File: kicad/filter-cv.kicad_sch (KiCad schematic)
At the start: 21 parts, among them Q11 2N3906, Q12 2N3904, Q13 2N3906, U18 TL074

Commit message: component positioning mostly done
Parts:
- C55, C56: footprint rumblesan-standard-parts:C_Rect_L7.0mm_W3.5mm_P5.00mm -> rumblesan-standard-parts:C_Rect_L7.0mm_W2.5mm_P5.00mm
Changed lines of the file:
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@@
       (effects (font (size 1.27 1.27)) (justify left))
     )
-    (property "Footprint" "rumblesan-standard-parts:C_Rect_L7.0mm_W3.5mm_P5.00mm" (id 2) (at 197.485 63.5 90)
+    (property "Footprint" "rumblesan-standard-parts:C_Rect_L7.0mm_W2.5mm_P5.00mm" (id 2) (at 197.485 63.5 90)
       (effects (font (size 1.27 1.27)) hide)
     )
@@
       (effects (font (size 1.27 1.27)) (justify left))
     )
-    (property "Footprint" "rumblesan-standard-parts:C_Rect_L7.0mm_W3.5mm_P5.00mm" (id 2) (at 197.485 76.2 90)
-      (effects (font (size 1.27 1.27)) hide)
-    )
+    (property "Footprint" "rumblesan-standard-parts:C_Rect_L7.0mm_W2.5mm_P5.00mm" (id 2) (at 197.485 76.2 90)
+      (effects (font (size 1.27 1.27)) hide)
+    )

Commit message: initial layout done
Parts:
- C53, C54: footprint rumblesan-standard-parts:C_Rect_L7.0mm_W3.5mm_P5.00mm -> rumblesan-standard-parts:C_Rect_L7.0mm_W2.5mm_P5.00mm
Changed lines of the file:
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@@
     (property "Reference" "C54" (id 0) (at 95.25 56.3712 90))
     (property "Value" "220pF" (id 1) (at 95.25 58.9081 90))
-    (property "Footprint" "rumblesan-standard-parts:C_Rect_L7.0mm_W3.5mm_P5.00mm" (id 2) (at 93.98 56.515 0)
+    (property "Footprint" "rumblesan-standard-parts:C_Rect_L7.0mm_W2.5mm_P5.00mm" (id 2) (at 93.98 56.515 0)
       (effects (font (size 1.27 1.27)) hide)
     )
@@
     (property "Reference" "C53" (id 0) (at 90.17 116.0612 90))
     (property "Value" "10nF" (id 1) (at 90.17 118.5981 90))
-    (property "Footprint" "rumblesan-standard-parts:C_Rect_L7.0mm_W3.5mm_P5.00mm" (id 2) (at 88.9 116.205 0)
-      (effects (font (size 1.27 1.27)) hide)
-    )
+    (property "Footprint" "rumblesan-standard-parts:C_Rect_L7.0mm_W2.5mm_P5.00mm" (id 2) (at 88.9 116.205 0)
+      (effects (font (size 1.27 1.27)) hide)
+    )

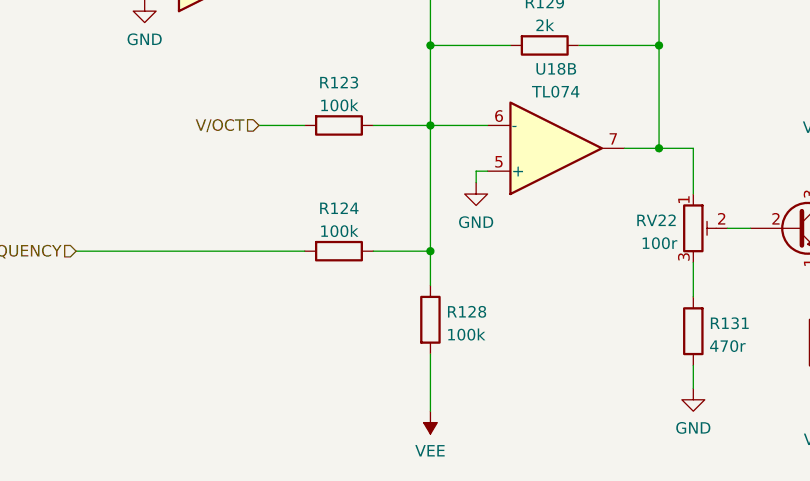
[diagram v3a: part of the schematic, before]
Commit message: Full rejig to use attiny for divider
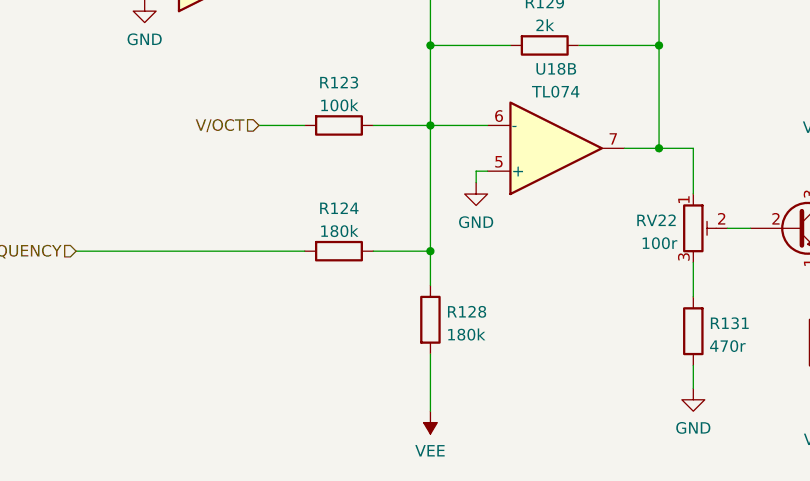
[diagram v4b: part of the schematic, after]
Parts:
- C55, C56: Spec ceramic C0G -> ceramic X7R
- R124, R128: value 100k -> 180k
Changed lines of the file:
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@@
       (effects (font (size 1.27 1.27)) hide)
     )
-    (property "Spec" "ceramic C0G" (id 4) (at 195.58 64.77 90)
+    (property "Spec" "ceramic X7R" (id 4) (at 195.58 64.77 90)
       (effects (font (size 1.27 1.27)) hide)
     )
@@
     (in_bom yes) (on_board yes) (fields_autoplaced)
     (property "Reference" "R124" (id 0) (at 67.31 148.9542 90))
-    (property "Value" "100k" (id 1) (at 67.31 151.4911 90))
+    (property "Value" "180k" (id 1) (at 67.31 151.4911 90))
     (property "Footprint" "rumblesan-standard-parts:R_Axial_DIN0207_L6.3mm_D2.5mm_P10.16mm_Horizontal" (id 2) (at 69.85 151.13 90)
       (effects (font (size 1.27 1.27)) hide)
@@
       (effects (font (size 1.27 1.27)) (justify right))
     )
-    (property "Value" "100k" (id 1) (at 79.248 162.9922 0)
+    (property "Value" "180k" (id 1) (at 79.248 162.9922 0)
       (effects (font (size 1.27 1.27)) (justify right))
     )
@@
       (effects (font (size 1.27 1.27)) hide)
     )
-    (property "Spec" "ceramic C0G" (id 4) (at 195.58 77.47 90)
-      (effects (font (size 1.27 1.27)) hide)
-    )
+    (property "Spec" "ceramic X7R" (id 4) (at 195.58 77.47 90)
+      (effects (font (size 1.27 1.27)) hide)
+    )

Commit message: Changing name to the mercurial machine
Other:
- title: (none) -> The Mercurial Machine
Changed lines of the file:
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@@
   (paper "A4")
   (title_block
+    (title "The Mercurial Machine")
+    (date "2023-05-13")
+    (rev "r02")
     (comment 2 "creativecommons.org/licenses/by/4.0/")
     (comment 3 "License: CC BY 4.0")

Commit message: geographically reannotate parts
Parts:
- renumbered C54 to C58, C55 to C59, C53 to C60, C56 to C65, Q12 to Q10, Q13 to Q9, R130 to R114, R131 to R115, R129 to R116, R123 to R119, R132 to R120, R127 to R122, R124 to R123, R121 to R126, R128 to R127, R122 to R128, R126 to R129, U18 to U16
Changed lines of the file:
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@@
   (symbol (lib_id "rumblesan-standard-parts:R") (at 106.68 162.56 0) (unit 1)
     (in_bom yes) (on_board yes) (fields_autoplaced)
-    (property "Reference" "R131" (id 0) (at 108.458 161.7253 0)
+    (property "Reference" "R115" (id 0) (at 108.458 161.7253 0)
       (effects (font (size 1.27 1.27)) (justify left))
     )
@@
   (symbol (lib_id "rumblesan-standard-parts:C") (at 191.77 64.77 0) (unit 1)
     (in_bom yes) (on_board yes) (fields_autoplaced)
-    (property "Reference" "C55" (id 0) (at 194.691 63.9353 0)
+    (property "Reference" "C59" (id 0) (at 194.691 63.9353 0)
       (effects (font (size 1.27 1.27)) (justify left))
     )
@@
   (symbol (lib_id "rumblesan-standard-parts:R") (at 120.65 163.83 0) (unit 1)
     (in_bom yes) (on_board yes) (fields_autoplaced)
-    (property "Reference" "R132" (id 0) (at 122.428 162.9953 0)
+    (property "Reference" "R120" (id 0) (at 122.428 162.9953 0)
       (effects (font (size 1.27 1.27)) (justify left))
     )
@@
   (symbol (lib_id "Amplifier_Operational:TL074") (at 185.42 71.12 0) (unit 5)
     (in_bom yes) (on_board yes) (fields_autoplaced)
-    (property "Reference" "U18" (id 0) (at 183.515 70.2853 0)
+    (property "Reference" "U16" (id 0) (at 183.515 70.2853 0)
       (effects (font (size 1.27 1.27)) (justify left))
     )
@@
   (symbol (lib_id "rumblesan-standard-parts:R") (at 90.17 130.81 90) (unit 1)
     (in_bom yes) (on_board yes) (fields_autoplaced)
-    (property "Reference" "R129" (id 0) (at 90.17 126.0942 90))
+    (property "Reference" "R116" (id 0) (at 90.17 126.0942 90))
     (property "Value" "2k" (id 1) (at 90.17 128.6311 90))
     (property "Footprint" "rumblesan-standard-parts:R_Axial_DIN0207_L6.3mm_D2.5mm_P10.16mm_Horizontal" (id 2) (at 92.71 128.27 90)
@@
   (symbol (lib_id "rumblesan-standard-parts:R") (at 67.31 153.67 90) (unit 1)
     (in_bom yes) (on_board yes) (fields_autoplaced)
-    (property "Reference" "R124" (id 0) (at 67.31 148.9542 90))
+    (property "Reference" "R123" (id 0) (at 67.31 148.9542 90))
     (property "Value" "180k" (id 1) (at 67.31 151.4911 90))
     (property "Footprint" "rumblesan-standard-parts:R_Axial_DIN0207_L6.3mm_D2.5mm_P10.16mm_Horizontal" (id 2) (at 69.85 151.13 90)
@@
   (symbol (lib_id "Amplifier_Operational:TL074") (at 54.61 121.92 0) (mirror x) (unit 3)
     (in_bom yes) (on_board yes) (fields_autoplaced)
-    (property "Reference" "U18" (id 0) (at 54.61 113.1402 0))
+    (property "Reference" "U16" (id 0) (at 54.61 113.1402 0))
     (property "Value" "TL074" (id 1) (at 54.61 115.6771 0))
     (property "Footprint" "rumblesan-standard-parts:DIP-14_W7.62mm_Socket" (id 2) (at 53.34 124.46 0)
@@
   (symbol (lib_id "rumblesan-standard-parts:R") (at 77.47 161.29 180) (unit 1)
     (in_bom yes) (on_board yes) (fields_autoplaced)
-    (property "Reference" "R128" (id 0) (at 79.248 160.4553 0)
+    (property "Reference" "R127" (id 0) (at 79.248 160.4553 0)
       (effects (font (size 1.27 1.27)) (justify right))
     )
@@
   (symbol (lib_id "Amplifier_Operational:TL074") (at 91.44 142.24 0) (mirror x) (unit 2)
     (in_bom yes) (on_board yes) (fields_autoplaced)
-    (property "Reference" "U18" (id 0) (at 91.44 133.4602 0))
+    (property "Reference" "U16" (id 0) (at 91.44 133.4602 0))
     (property "Value" "TL074" (id 1) (at 91.44 135.9971 0))
     (property "Footprint" "rumblesan-standard-parts:DIP-14_W7.62mm_Socket" (id 2) (at 90.17 144.78 0)
@@
   (symbol (lib_id "rumblesan-standard-parts:R") (at 54.61 38.1 90) (unit 1)
     (in_bom yes) (on_board yes) (fields_autoplaced)
-    (property "Reference" "R121" (id 0) (at 54.61 33.3842 90))
+    (property "Reference" "R126" (id 0) (at 54.61 33.3842 90))
     (property "Value" "20k" (id 1) (at 54.61 35.9211 90))
     (property "Footprint" "rumblesan-standard-parts:R_Axial_DIN0207_L6.3mm_D2.5mm_P10.16mm_Horizontal" (id 2) (at 57.15 35.56 90)
@@
   (symbol (lib_id "Transistor_BJT:2N3904") (at 118.11 151.13 0) (unit 1)
     (in_bom yes) (on_board yes) (fields_autoplaced)
-    (property "Reference" "Q12" (id 0) (at 122.9614 150.2953 0)
+    (property "Reference" "Q10" (id 0) (at 122.9614 150.2953 0)
       (effects (font (size 1.27 1.27)) (justify left))
     )
@@
   (symbol (lib_id "rumblesan-standard-parts:R") (at 100.33 52.07 90) (unit 1)
     (in_bom yes) (on_board yes) (fields_autoplaced)
-    (property "Reference" "R130" (id 0) (at 100.33 47.3542 90))
+    (property "Reference" "R114" (id 0) (at 100.33 47.3542 90))
     (property "Value" "20k" (id 1) (at 100.33 49.8911 90))
     (property "Footprint" "rumblesan-standard-parts:R_Axial_DIN0207_L6.3mm_D2.5mm_P10.16mm_Horizontal" (id 2) (at 102.87 49.53 90)
@@
   (symbol (lib_id "rumblesan-standard-parts:C") (at 95.25 62.23 90) (unit 1)
     (in_bom yes) (on_board yes) (fields_autoplaced)
-    (property "Reference" "C54" (id 0) (at 95.25 56.3712 90))
+    (property "Reference" "C58" (id 0) (at 95.25 56.3712 90))
     (property "Value" "220pF" (id 1) (at 95.25 58.9081 90))
     (property "Footprint" "rumblesan-standard-parts:C_Rect_L7.0mm_W2.5mm_P5.00mm" (id 2) (at 93.98 56.515 0)
@@
   (symbol (lib_id "rumblesan-standard-parts:C") (at 191.77 77.47 0) (unit 1)
     (in_bom yes) (on_board yes) (fields_autoplaced)
-    (property "Reference" "C56" (id 0) (at 194.691 76.6353 0)
+    (property "Reference" "C65" (id 0) (at 194.691 76.6353 0)
       (effects (font (size 1.27 1.27)) (justify left))
     )
@@
   (symbol (lib_id "Transistor_BJT:2N3906") (at 133.35 158.75 0) (unit 1)
     (in_bom yes) (on_board yes) (fields_autoplaced)
-    (property "Reference" "Q13" (id 0) (at 138.2014 157.9153 0)
+    (property "Reference" "Q9" (id 0) (at 138.2014 157.9153 0)
       (effects (font (size 1.27 1.27)) (justify left))
     )
@@
   (symbol (lib_id "Amplifier_Operational:TL074") (at 95.25 76.2 0) (mirror x) (unit 1)
     (in_bom yes) (on_board yes) (fields_autoplaced)
-    (property "Reference" "U18" (id 0) (at 95.25 67.4202 0))
+    (property "Reference" "U16" (id 0) (at 95.25 67.4202 0))
     (property "Value" "TL074" (id 1) (at 95.25 69.9571 0))
     (property "Footprint" "rumblesan-standard-parts:DIP-14_W7.62mm_Socket" (id 2) (at 93.98 78.74 0)
@@
   (symbol (lib_id "rumblesan-standard-parts:C") (at 90.17 121.92 90) (unit 1)
     (in_bom yes) (on_board yes) (fields_autoplaced)
-    (property "Reference" "C53" (id 0) (at 90.17 116.0612 90))
+    (property "Reference" "C60" (id 0) (at 90.17 116.0612 90))
     (property "Value" "10nF" (id 1) (at 90.17 118.5981 90))
     (property "Footprint" "rumblesan-standard-parts:C_Rect_L7.0mm_W2.5mm_P5.00mm" (id 2) (at 88.9 116.205 0)
@@
   (symbol (lib_id "Amplifier_Operational:TL074") (at 54.61 53.34 0) (mirror x) (unit 4)
     (in_bom yes) (on_board yes) (fields_autoplaced)
-    (property "Reference" "U18" (id 0) (at 54.61 44.5602 0))
+    (property "Reference" "U16" (id 0) (at 54.61 44.5602 0))
     (property "Value" "TL074" (id 1) (at 54.61 47.0971 0))
     (property "Footprint" "rumblesan-standard-parts:DIP-14_W7.62mm_Socket" (id 2) (at 53.34 55.88 0)
@@
   (symbol (lib_id "rumblesan-standard-parts:R") (at 72.39 73.66 90) (unit 1)
     (in_bom yes) (on_board yes) (fields_autoplaced)
-    (property "Reference" "R127" (id 0) (at 72.39 68.9442 90))
+    (property "Reference" "R122" (id 0) (at 72.39 68.9442 90))
     (property "Value" "100k" (id 1) (at 72.39 71.4811 90))
     (property "Footprint" "rumblesan-standard-parts:R_Axial_DIN0207_L6.3mm_D2.5mm_P10.16mm_Horizontal" (id 2) (at 74.93 71.12 90)
@@
   (symbol (lib_id "rumblesan-standard-parts:R") (at 67.31 139.7 90) (unit 1)
     (in_bom yes) (on_board yes) (fields_autoplaced)
-    (property "Reference" "R123" (id 0) (at 67.31 134.9842 90))
+    (property "Reference" "R119" (id 0) (at 67.31 134.9842 90))
     (property "Value" "100k" (id 1) (at 67.31 137.5211 90))
     (property "Footprint" "rumblesan-standard-parts:R_Axial_DIN0207_L6.3mm_D2.5mm_P10.16mm_Horizontal" (id 2) (at 69.85 137.16 90)
@@
   (symbol (lib_id "rumblesan-standard-parts:R") (at 54.61 109.22 90) (unit 1)
     (in_bom yes) (on_board yes)
-    (property "Reference" "R122" (id 0) (at 54.61 104.5042 90))
+    (property "Reference" "R128" (id 0) (at 54.61 104.5042 90))
     (property "Value" "100k" (id 1) (at 54.61 107.0411 90))
     (property "Footprint" "rumblesan-standard-parts:R_Axial_DIN0207_L6.3mm_D2.5mm_P10.16mm_Horizontal" (id 2) (at 57.15 106.68 90)
@@
   (symbol (lib_id "rumblesan-standard-parts:R") (at 71.12 121.92 90) (unit 1)
     (in_bom yes) (on_board yes) (fields_autoplaced)
-    (property "Reference" "R126" (id 0) (at 71.12 117.2042 90))
+    (property "Reference" "R129" (id 0) (at 71.12 117.2042 90))
     (property "Value" "100k" (id 1) (at 71.12 119.7411 90))
     (property "Footprint" "rumblesan-standard-parts:R_Axial_DIN0207_L6.3mm_D2.5mm_P10.16mm_Horizontal" (id 2) (at 73.66 119.38 90)

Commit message: Changing name again
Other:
- title: The Mercurial Machine -> Ouroboros
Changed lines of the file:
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@@
   (paper "A4")
   (title_block
-    (title "The Mercurial Machine")
+    (title "Ouroboros")
     (date "2023-05-13")
     (rev "r02")
